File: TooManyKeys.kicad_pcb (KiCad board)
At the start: 2 copper layers, 156 x 116.5 mm, 89 parts, among them U1 TLV61070ADBV, U2 SN74LV1T126DBVR

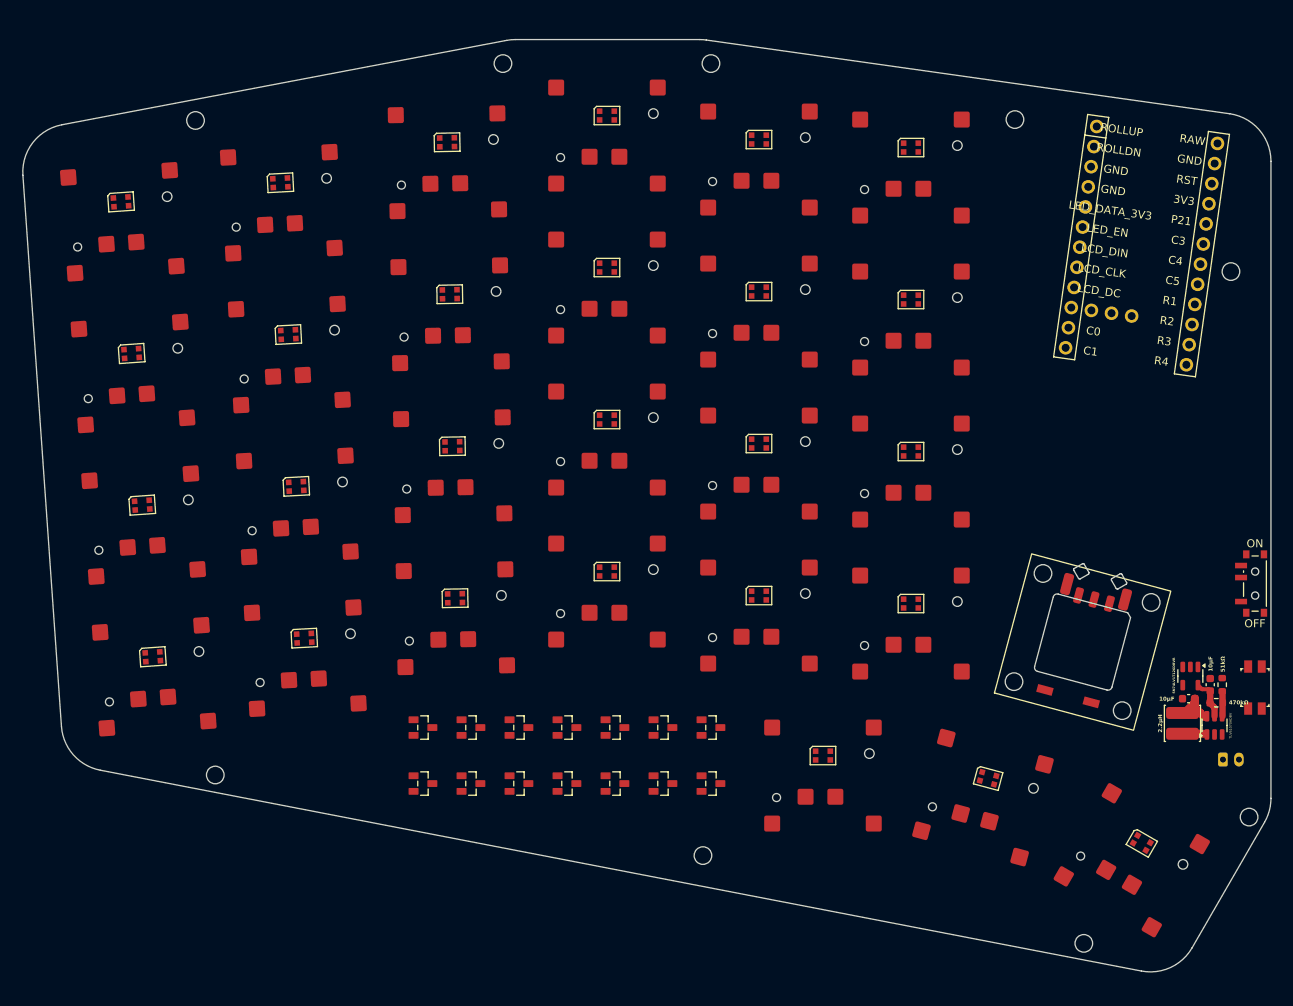
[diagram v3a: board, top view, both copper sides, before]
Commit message: Complete draft 3 of routing, near complete. Fix pad positions on roller encoder.
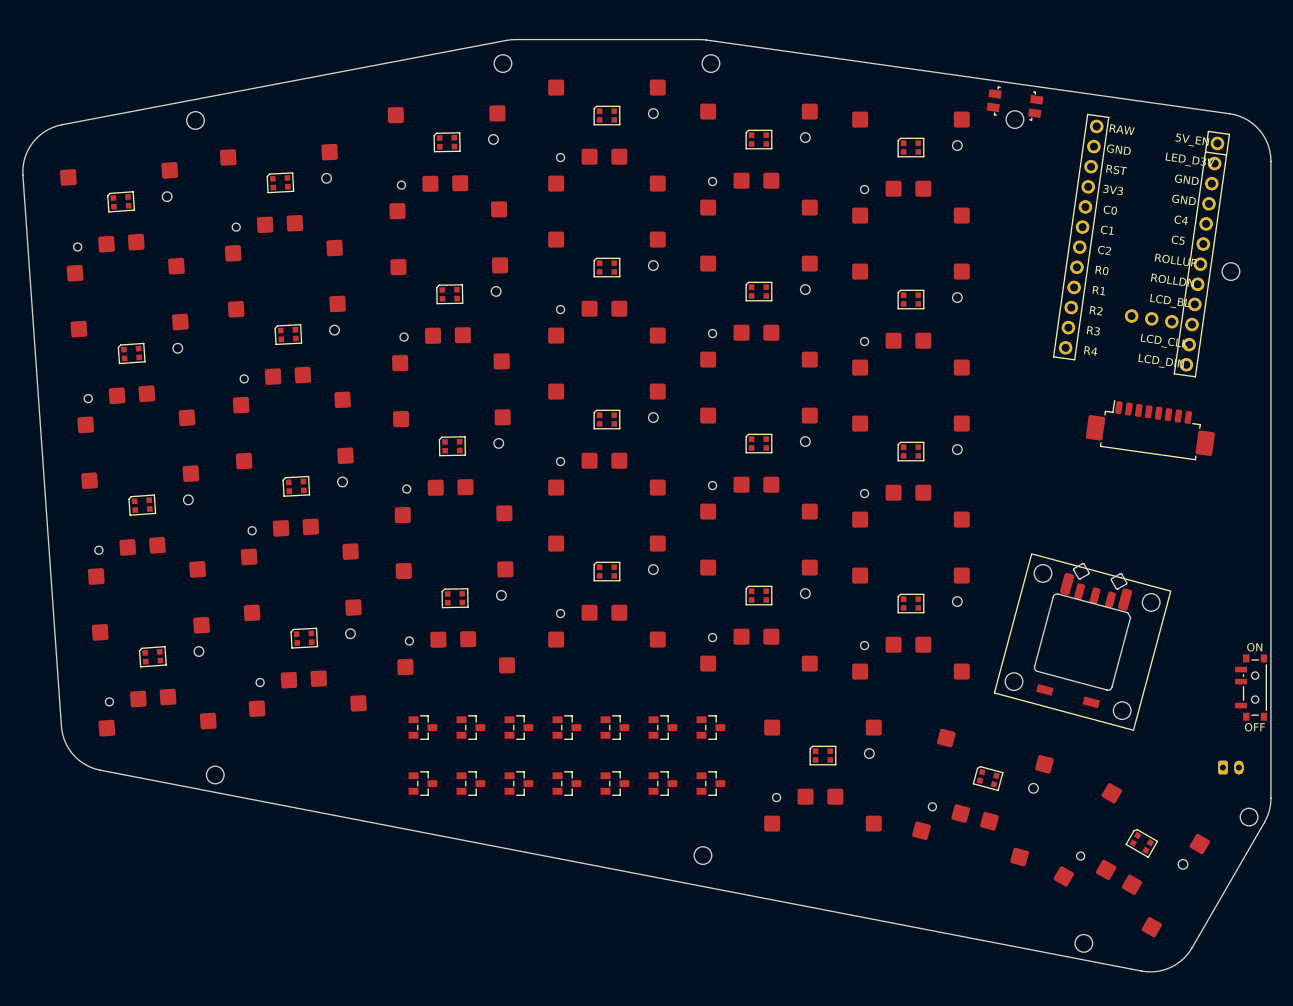
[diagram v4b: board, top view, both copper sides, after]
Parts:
- removed C1, C2: 10μF, Capacitor_SMD:C_0603_1608Metric
- removed L1: 2.2μH, huntercook:L_CJIANG_FTC404030S_4.1x4.1x3.0_SMD
- removed R1: 470kΩ, Resistor_SMD:R_0603_1608Metric
- removed R2: 51kΩ, Resistor_SMD:R_0603_1608Metric
- removed U1: TLV61070ADBV, Package_TO_SOT_SMD:SOT-23-6
- removed U2: SN74LV1T126DBVR, Package_TO_SOT_SMD:SOT-23-5
- added CONN1: , Molex_PicoBlade_53261-0871_1x08-1MP_P1.25mm_Horizontal, F.Cu at (184.6, 129.4)
- moved RST1 78.9 mm to (167.6, 88.4), turned to -8 degrees
- moved D7 36.7 mm to (93.6, 173.4)
- moved PWR1 13.0 mm to (197.6, 161.4)
- moved D13 9.22 mm to (129.6, 166.4)
- moved D10 6.00 mm to (111.6, 173.4)
- moved D11 6.00 mm to (117.6, 173.4)
- moved D12 6.00 mm to (123.6, 173.4)
- moved D8 6.00 mm to (99.6, 173.4)
- moved D9 6.00 mm to (105.6, 173.4)
- moved JST1 1.00 mm to (194.6, 171.4)
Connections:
- net LED_PWR renamed 5V
- D1 pad 1: finger_outer_num -> finger_pinky_num
- D1 pad 2: finger_pinky_num -> finger_outer_num
- D1 pad 3: R1 -> R0
- D10 pad 1: finger_outer_bottom -> finger_pinky_bottom
- D10 pad 3: R1 -> R3
- D11 pad 1: finger_ring_bottom -> finger_middle_bottom
- D11 pad 2: finger_middle_bottom -> finger_ring_bottom
- D11 pad 3: R1 -> R3
- D12 pad 1: finger_index_bottom -> finger_inner_bottom
- D12 pad 2: finger_inner_bottom -> finger_index_bottom
- D12 pad 3: R1 -> R3
- D13 pad 1: thumb_near_fan -> roller
- D13 pad 2: thumb_mid_fan -> thumb_near_fan
- D13 pad 3: R1 -> R4
- D14 pad 1: thumb_far_fan -> thumb_mid_fan
- D14 pad 2: roller -> thumb_far_fan
- D14 pad 3: R1 -> R4
- D2 pad 1: finger_ring_num -> finger_middle_num
- D2 pad 2: finger_middle_num -> finger_ring_num
- D2 pad 3: R1 -> R0
- D3 pad 1: finger_index_num -> finger_inner_num
- D3 pad 2: finger_inner_num -> finger_index_num
- D3 pad 3: R1 -> R0
- D4 pad 1: finger_outer_top -> finger_pinky_top
- D5 pad 1: finger_ring_top -> finger_middle_top
- D5 pad 2: finger_middle_top -> finger_ring_top
- D6 pad 1: finger_index_top -> finger_inner_top
- D6 pad 2: finger_inner_top -> finger_index_top
- D7 pad 1: finger_outer_home -> finger_pinky_home
- D7 pad 3: R1 -> R2
- D8 pad 1: finger_ring_home -> finger_middle_home
- D8 pad 2: finger_middle_home -> finger_ring_home
- D8 pad 3: R1 -> R2
- D9 pad 1: finger_index_home -> finger_inner_home
- D9 pad 2: finger_inner_home -> finger_index_home
- D9 pad 3: R1 -> R2
- LED27 pad 1: LED_DATA_5V -> LED_D5V
- MCU1 pad 1: RAW -> 5V_EN
- MCU1 pad 10: R2 -> LCD_DC
- MCU1 pad 11: R3 -> LCD_CLK
- MCU1 pad 12: R4 -> LCD_DIN
- MCU1 pad 13: C1 -> R4
- MCU1 pad 14: C0 -> R3
- MCU1 pad 15: LCD_BL -> R2
- MCU1 pad 16: LCD_DC -> R1
- MCU1 pad 17: LCD_CLK -> R0
- MCU1 pad 18: LCD_DIN -> C2
- MCU1 pad 19: LED_EN -> C1
- MCU1 pad 2: GND -> LED_D3V
- MCU1 pad 20: LED_DATA_3V3 -> C0
- MCU1 pad 21: GND -> 3V3
- MCU1 pad 22: GND -> RST
- MCU1 pad 23: ROLLDN -> GND
- MCU1 pad 24: ROLLUP -> RAW
- MCU1 pad 25: LCD_CS -> LCD_RST
- MCU1 pad 26: LCD_RST -> LCD_CS
- MCU1 pad 27: C2 -> C3
- MCU1 pad 3: RST -> GND
- MCU1 pad 4: 3V3 -> GND
- MCU1 pad 5: P21 -> C4
- MCU1 pad 6: C3 -> C5
- MCU1 pad 7: C4 -> ROLLUP
- MCU1 pad 8: C5 -> ROLLDN
- MCU1 pad 9: R1 -> LCD_BL
- PWR1 pad 2: RAW -> BAT_P
- PWR1 pad 3: BAT_P -> RAW
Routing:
- net RAW: track 7.58 -> 0.00 mm
- net V_OUT: track 5.28 -> 0.00 mm
- net Net-(U1-V_{FB}): track 3.14 -> 0.00 mm
- net Net-(U1-SW): track 2.75 -> 0.00 mm

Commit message: Add LCD outline to board, move other components as needed. Add 3D model support to several footprints, add model for CKW12 roller encoder.
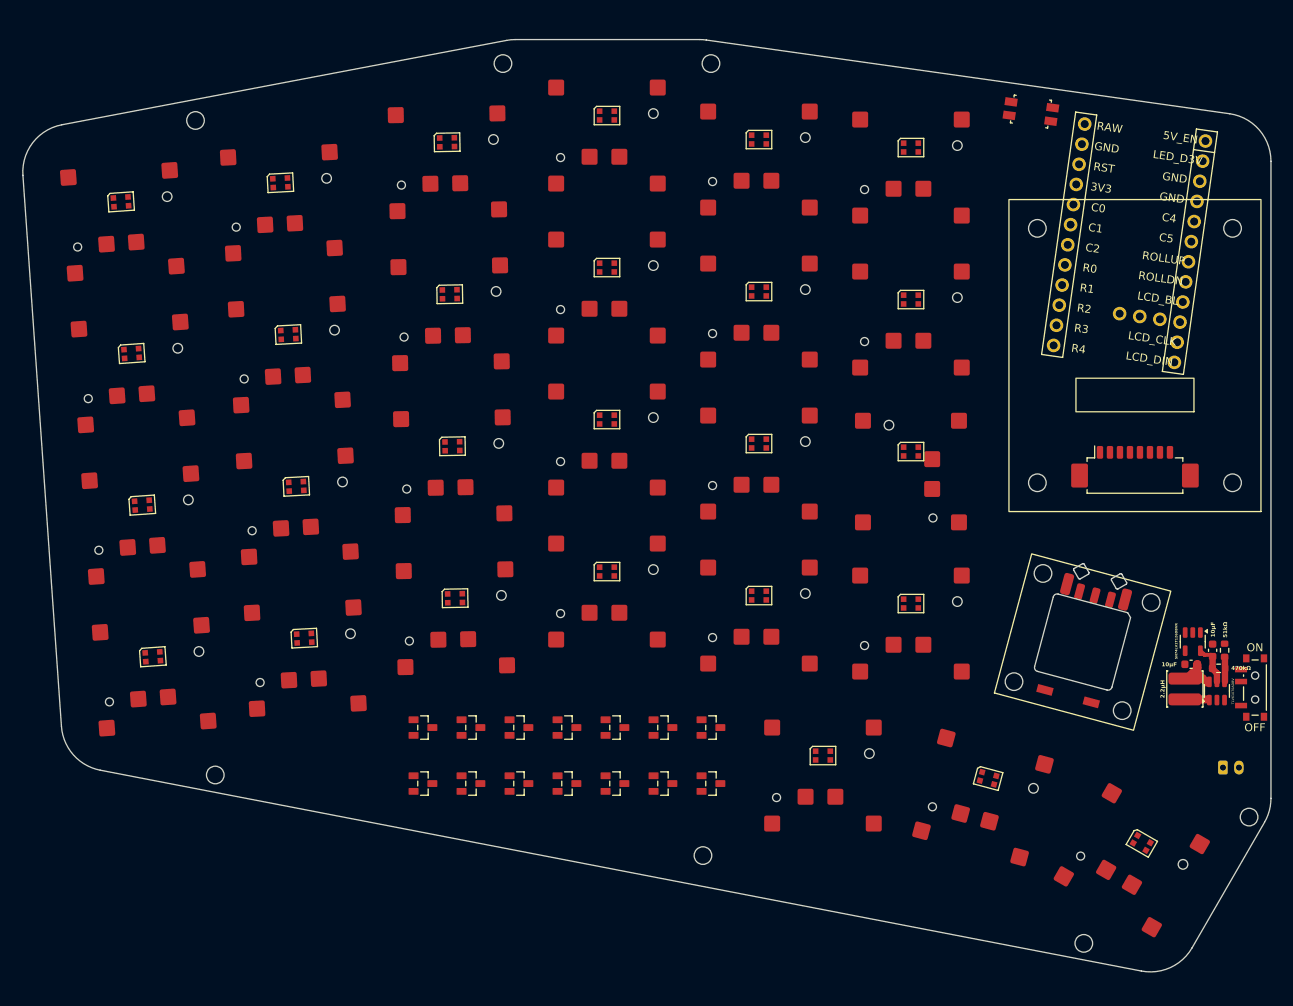
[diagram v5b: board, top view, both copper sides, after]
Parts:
- removed MH8, MH9: , ceoloide:mounting_hole_npth
- added C1: 10μF, Capacitor_SMD:C_0603_1608Metric, F.Cu at (189.6, 158.4)
- added C2: 10μF, Capacitor_SMD:C_0603_1608Metric, F.Cu at (192.3, 156.7)
- added L1: 2.2μH, huntercook:L_CJIANG_FTC404030S_4.1x4.1x3.0_SMD, F.Cu at (188.8, 161.5)
- added LCD1: , LCD_1.69_Waveshare, F.Cu at (182.6, 119.9)
- added R1: 470kΩ, Resistor_SMD:R_0603_1608Metric, F.Cu at (193.1, 159.0)
- added R2: 51kΩ, Resistor_SMD:R_0603_1608Metric, F.Cu at (193.8, 156.7)
- added U1: TLV61070ADBV, Package_TO_SOT_SMD:SOT-23-6, F.Cu at (192.8, 161.8)
- added U2: SN74LV1T126DBVR, Package_TO_SOT_SMD:SOT-23-5, F.Cu at (189.8, 155.6)
- moved MH5 99.9 mm to (128.6, 182.4)
- moved MH6 86.0 mm to (176.2, 193.3), turned to -30 degrees
- moved MH7 68.4 mm to (196.9, 177.5), turned to -30 degrees
- moved D1 7.00 mm to (93.6, 173.4)
- moved D2 7.00 mm to (99.6, 173.4)
- moved D3 7.00 mm to (105.6, 173.4)
- moved D4 7.00 mm to (111.6, 173.4)
- moved D5 7.00 mm to (117.6, 173.4)
- moved D6 7.00 mm to (123.6, 173.4)
- moved D10 7.00 mm to (111.6, 166.4)
- moved D11 7.00 mm to (117.6, 166.4)
- moved D12 7.00 mm to (123.6, 166.4)
- moved D7 7.00 mm to (93.6, 166.4)
- moved D8 7.00 mm to (99.6, 166.4)
- moved D9 7.00 mm to (105.6, 166.4)
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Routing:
- net RAW: track 0.00 -> 7.58 mm
- net 5V: track 0.00 -> 5.28 mm
- net BOOST_FB: track 0.00 -> 3.14 mm
- net BOOST_SW: track 0.00 -> 2.75 mm

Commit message: Work on power routing/design. Current thinking in main PCB file.
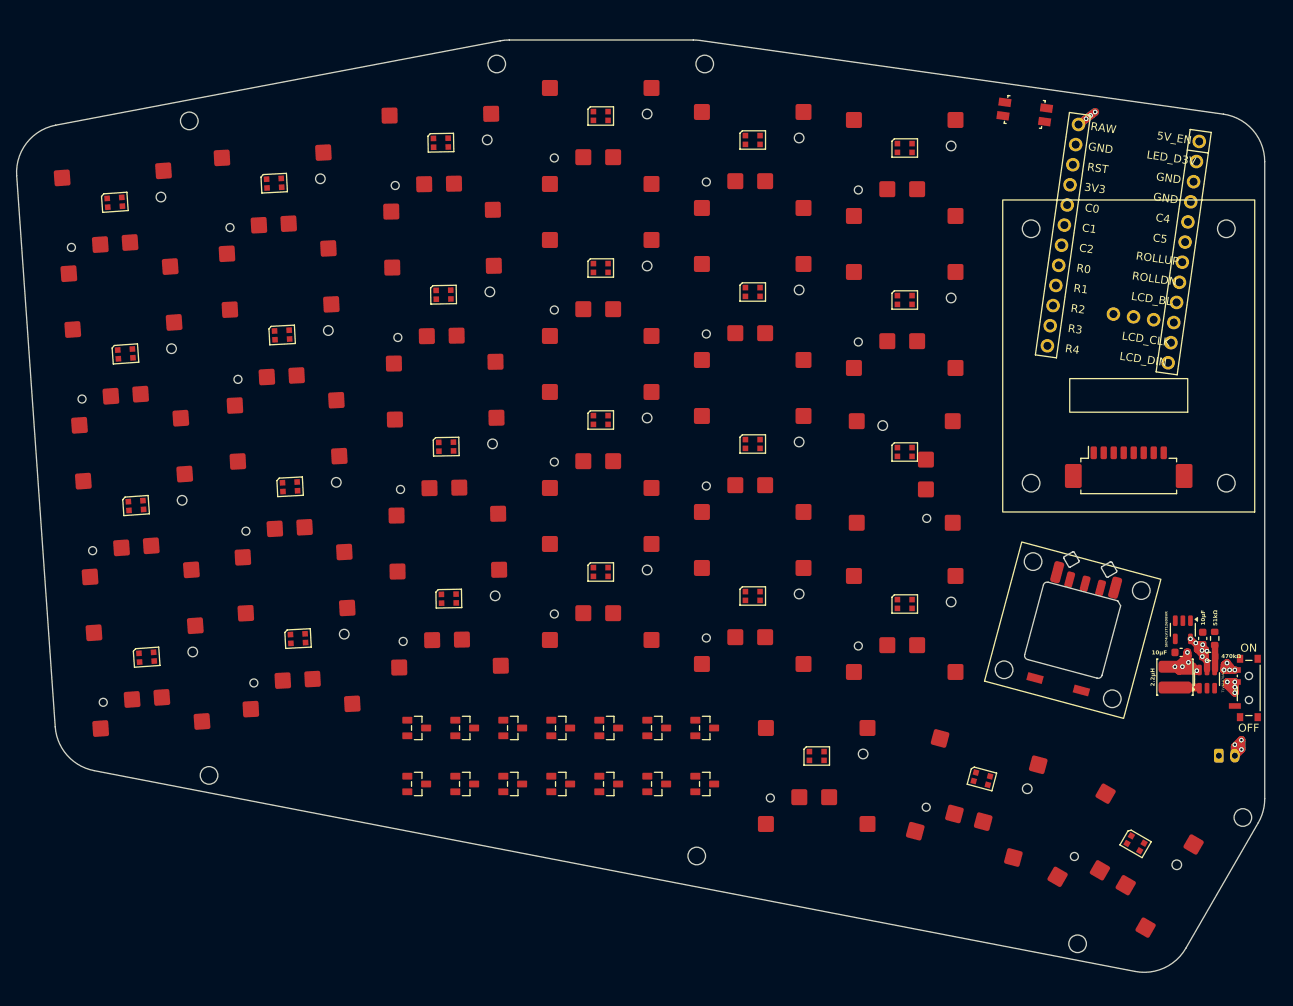
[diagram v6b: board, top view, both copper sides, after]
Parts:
- moved U1 1.93 mm to (191.6, 160.3)
- moved C1 1.93 mm to (188.4, 157.0)
- moved C2 1.93 mm to (191.1, 155.2)
- moved R2 1.93 mm to (192.6, 155.2)
- moved U2 1.93 mm to (188.6, 154.1)
- moved L1 1.93 mm to (187.6, 160.1)
- moved R1 1.93 mm to (191.8, 157.5)
- moved RE1 1.93 mm to (174.8, 154.2)
- moved JST1 1.57 mm to (194.1, 169.9)
- moved D1 0.78 mm to (92.8, 173.4)
- moved D11 0.78 mm to (116.8, 166.4)
- moved D3 0.78 mm to (104.8, 173.4)
- moved D6 0.78 mm to (122.8, 173.4)
- moved D8 0.78 mm to (98.8, 166.4)
- moved LED13 0.78 mm to (115.8, 146.9)
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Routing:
- net RAW: track 7.58 -> 130.4 mm, vias 0 -> 12
- net BAT_P: track 0.00 -> 30.0 mm, vias 0 -> 7
- net 5V: track 5.28 -> 13.5 mm, vias 0 -> 7
- added copper zone on In2.Cu, net 5V
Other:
- copper layers 2 -> 6

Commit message: Fix whatever boneheaded thing I did to mess up all the boostier pads.
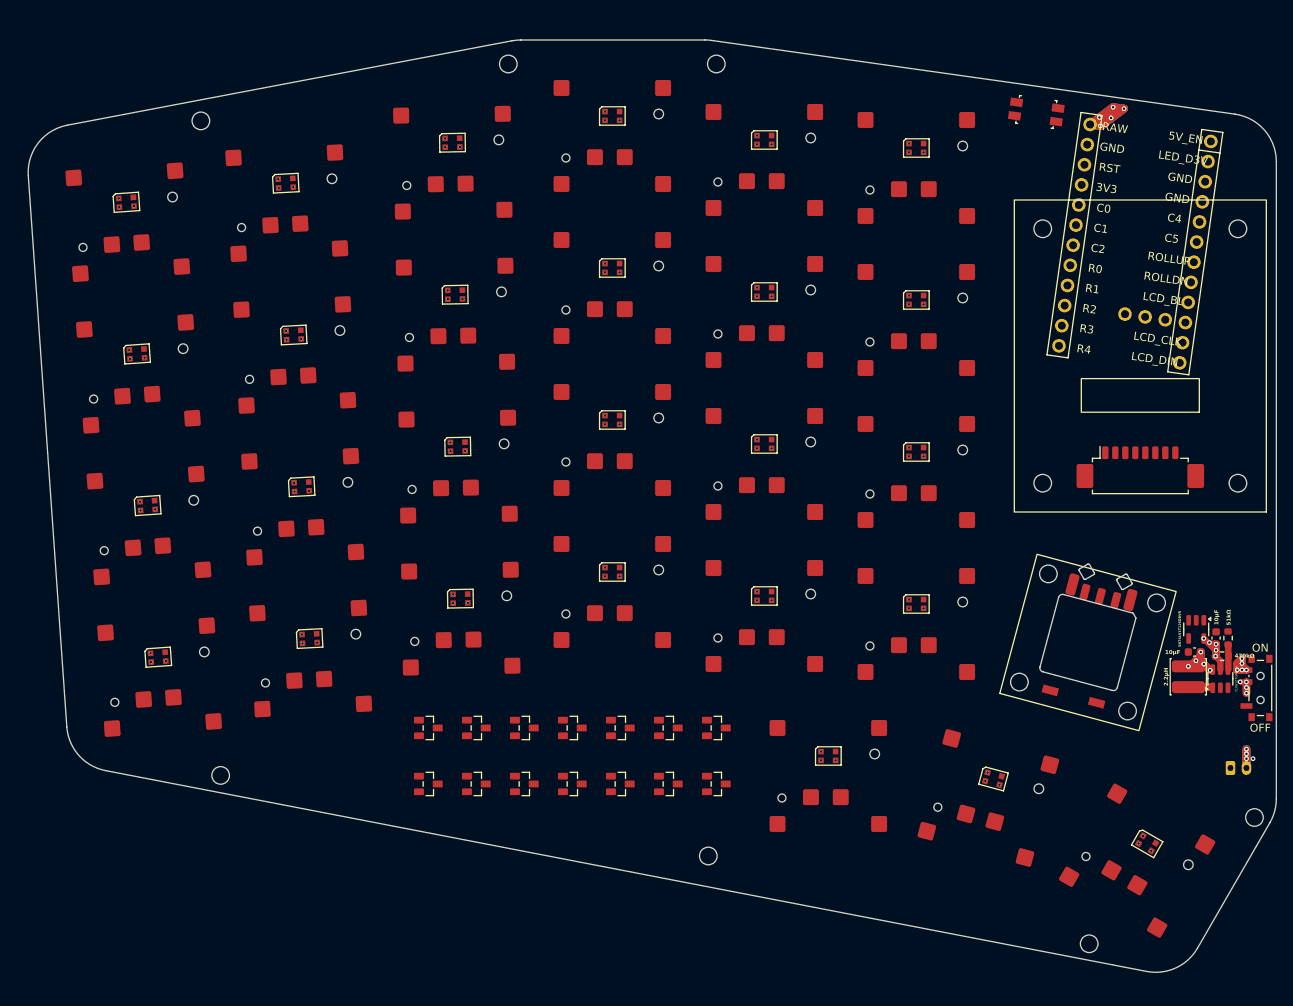
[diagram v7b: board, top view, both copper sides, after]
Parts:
- moved RE1 2.45 mm to (176.7, 155.7)
- moved JST1 2.11 mm to (195.5, 171.4)
- moved U1 1.67 mm to (193.3, 160.3)
- moved R2 1.67 mm to (194.2, 155.2)
- moved R1 1.67 mm to (193.5, 157.4)
- moved L1 1.67 mm to (189.3, 160.0)
- moved C1 1.67 mm to (190.0, 156.9)
- moved C2 1.67 mm to (192.7, 155.2)
- moved U2 1.67 mm to (190.3, 154.1)
- moved LED26 1.45 mm to (164.9, 172.7)
- moved MH7 1.45 mm to (197.5, 177.6)
- moved D1 1.45 mm to (94.3, 173.4)
- moved D10 1.45 mm to (112.3, 166.4)
- moved D11 1.45 mm to (118.3, 166.4)
- moved D12 1.45 mm to (124.3, 166.4)
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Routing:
- net RAW: track 130.4 -> 145.3 mm, vias 12 -> 15
- net BAT_P: track 30.0 -> 22.8 mm, vias 7 -> 8
- net 5V: track 13.5 -> 10.9 mm, vias 7 -> 5
- added copper zone on In1.Cu, net 5V
- removed copper zone on In2.Cu, net 5V
